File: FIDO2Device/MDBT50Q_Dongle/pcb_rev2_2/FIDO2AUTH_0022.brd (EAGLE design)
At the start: 19.5 x 34.3 mm, 40 parts, among them CN1 TE-1734028, CN2 IF_5PIN_H, SW1 SKRPACE010, SW2 SKTADAE010, U1 MDBT50Q-P1M, U2 XC6206P302MR-G, U4 RV-3028-C7, X1 NX3215SA-32.768K

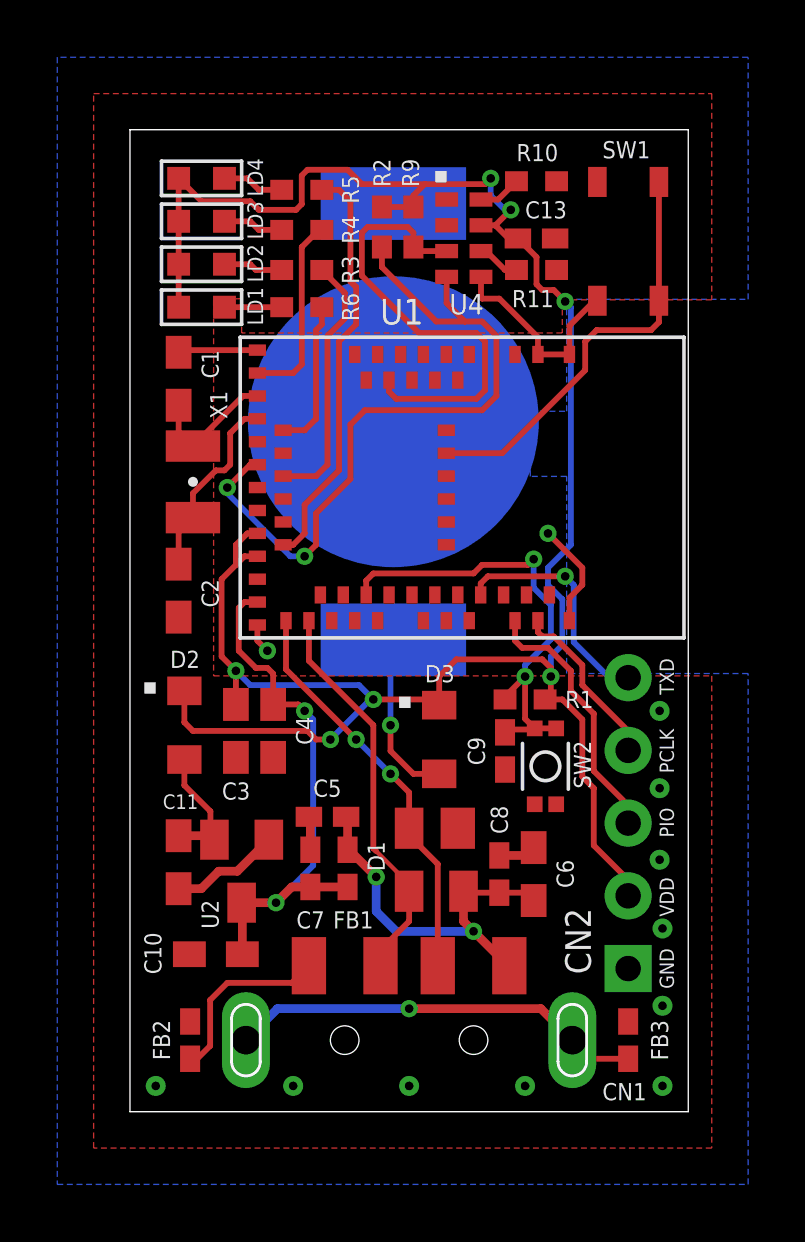
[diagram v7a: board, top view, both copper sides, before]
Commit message: 配線レイアウトを修正
・軽微な調整
・振り直した部品番号を反映
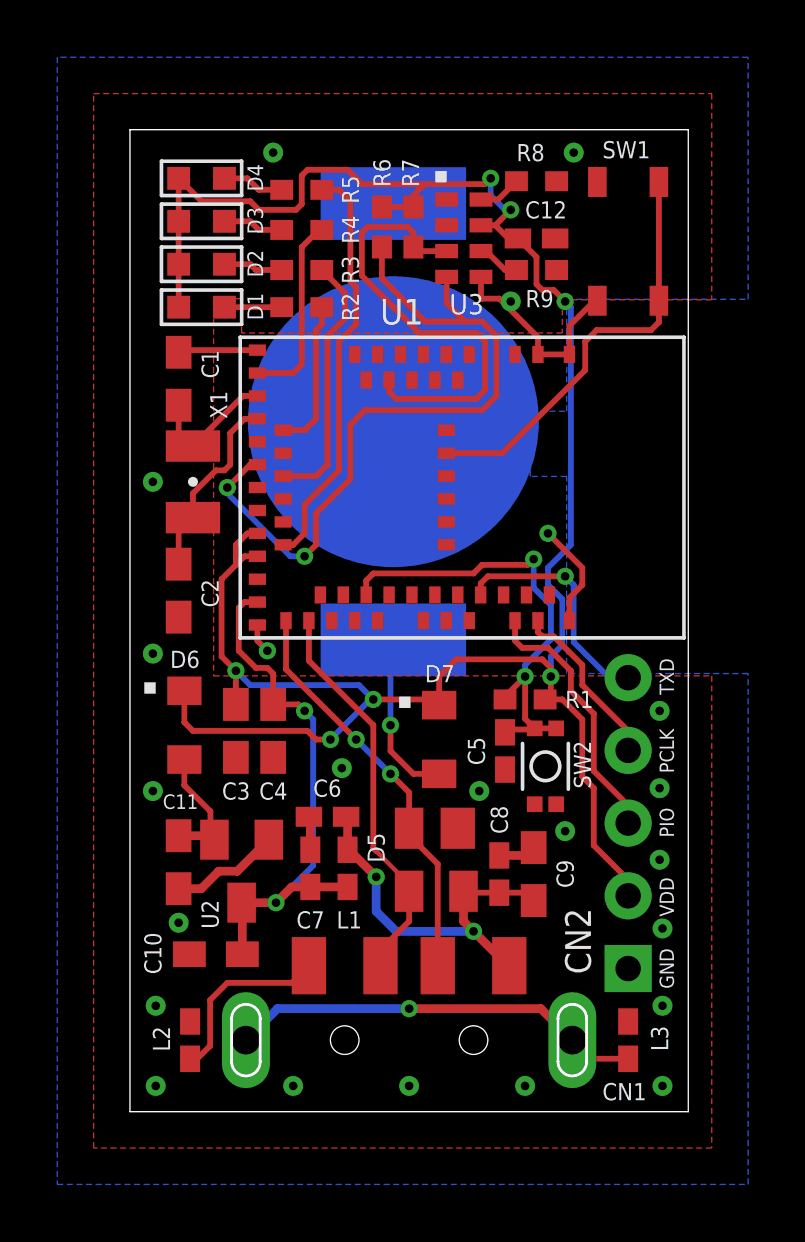
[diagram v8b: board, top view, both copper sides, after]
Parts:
- removed LD1: APTD1608LSECK/J4-PF, Parts:APTD1608
- removed LD2: APHD1608LSURCK, Parts:APTD1608
- removed LD3: APTD1608LZGCK, Parts:APTD1608
- removed R11: 10k, Parts:R0402N
- added D5: PRTR5V0U2X, Parts:SOT143B
- added D6, D7: PMEG2005AEA,115, Parts:SOD323-W
- added R7: 10k, Parts:R0402N
- C5: value 0.01uF -> 0.1uF
- C6: value 10uF -> 0.01uF; device Parts:C0603N -> Parts:C0402N
- C9: value 0.1uF -> 10uF; device Parts:C0402N -> Parts:C0603N
- D1: value PRTR5V0U2X -> APTD1608LSECK/J4-PF; device Parts:SOT143B -> Parts:APTD1608
- D2: value PMEG2005AEA,115 -> APHD1608LSURCK; device Parts:SOD323-W -> Parts:APTD1608
- D3: value PMEG2005AEA,115 -> APTD1608LZGCK; device Parts:SOD323-W -> Parts:APTD1608
- R2: value 10k -> 1.2k
- R6: value 1.2k -> 10k
- moved D1 21.0 mm to (2.50, 28.1), turned to 0 degrees
- moved D3 19.9 mm to (2.50, 31.1), turned to 0 degrees
- moved D2 16.1 mm to (2.50, 29.6), turned to 0 degrees
- moved C6 7.47 mm to (6.90, 10.3), turned to 180 degrees
- moved C5 6.61 mm to (13.1, 12.6), turned to 270 degrees
- moved R9 4.55 mm to (14.2, 29.4), turned to 180 degrees
- moved C9 4.41 mm to (14.1, 8.30), turned to 90 degrees
- moved R2 3.96 mm to (6.00, 28.1), turned to 180 degrees
- moved R6 3.96 mm to (8.80, 30.9), turned to 90 degrees
- renumbered C13 to C12, FB1 to L1, FB2 to L2, FB3 to L3, LD4 to D4, R10 to R8, U4 to U3
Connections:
- net 0V: now also D5.1, R9.1; no longer D1.1, R11.1
- net D_N: now also D5.2; no longer D1.2
- net D_P: now also D5.3; no longer D1.3
- net LED1: now also R2.1; no longer R6.1
- net N$4: now also D6.A; no longer D2.A
- net N$5: now also D7.A; no longer D3.A
- net N$6: now also D3.C; no longer LD3.C
- net N$7: now also D2.C; no longer LD2.C
- net N$8: now also D1.C, R2.2; no longer LD1.C, R6.2
- net N$9: now also R9.2; no longer R11.2
- net RESET: now also C5.1; no longer C9.1
- net TWI_SCL: now also R7.1; no longer R9.1
- net TWI_SDA: now also R6.1; no longer R2.1
- net VBUS: now also C9.1, D5.4; no longer C5.1, D1.4
- net VDD_NRF: now also D1.A, D2.A, D3.A, D6.C, D7.C, R6.2, R7.2; no longer D2.C, D3.C, LD1.A, LD2.A, LD3.A, R2.2, R9.2
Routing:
- net 0V: vias 12 -> 23
